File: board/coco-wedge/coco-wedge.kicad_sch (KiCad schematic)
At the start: 19 parts, among them J1 Foxconn_WQ21823-DES1-7F, J2 ZX-TYPEC-WCM1648, J3 Conn_ARM_JTAG_SWD_10, SW1 SW_Push, SW2 SW_SPDT, U1 AMS1117-3.3, U2 STM32G0B0RETx, U3 74LVC1G07, Y1 Crystal

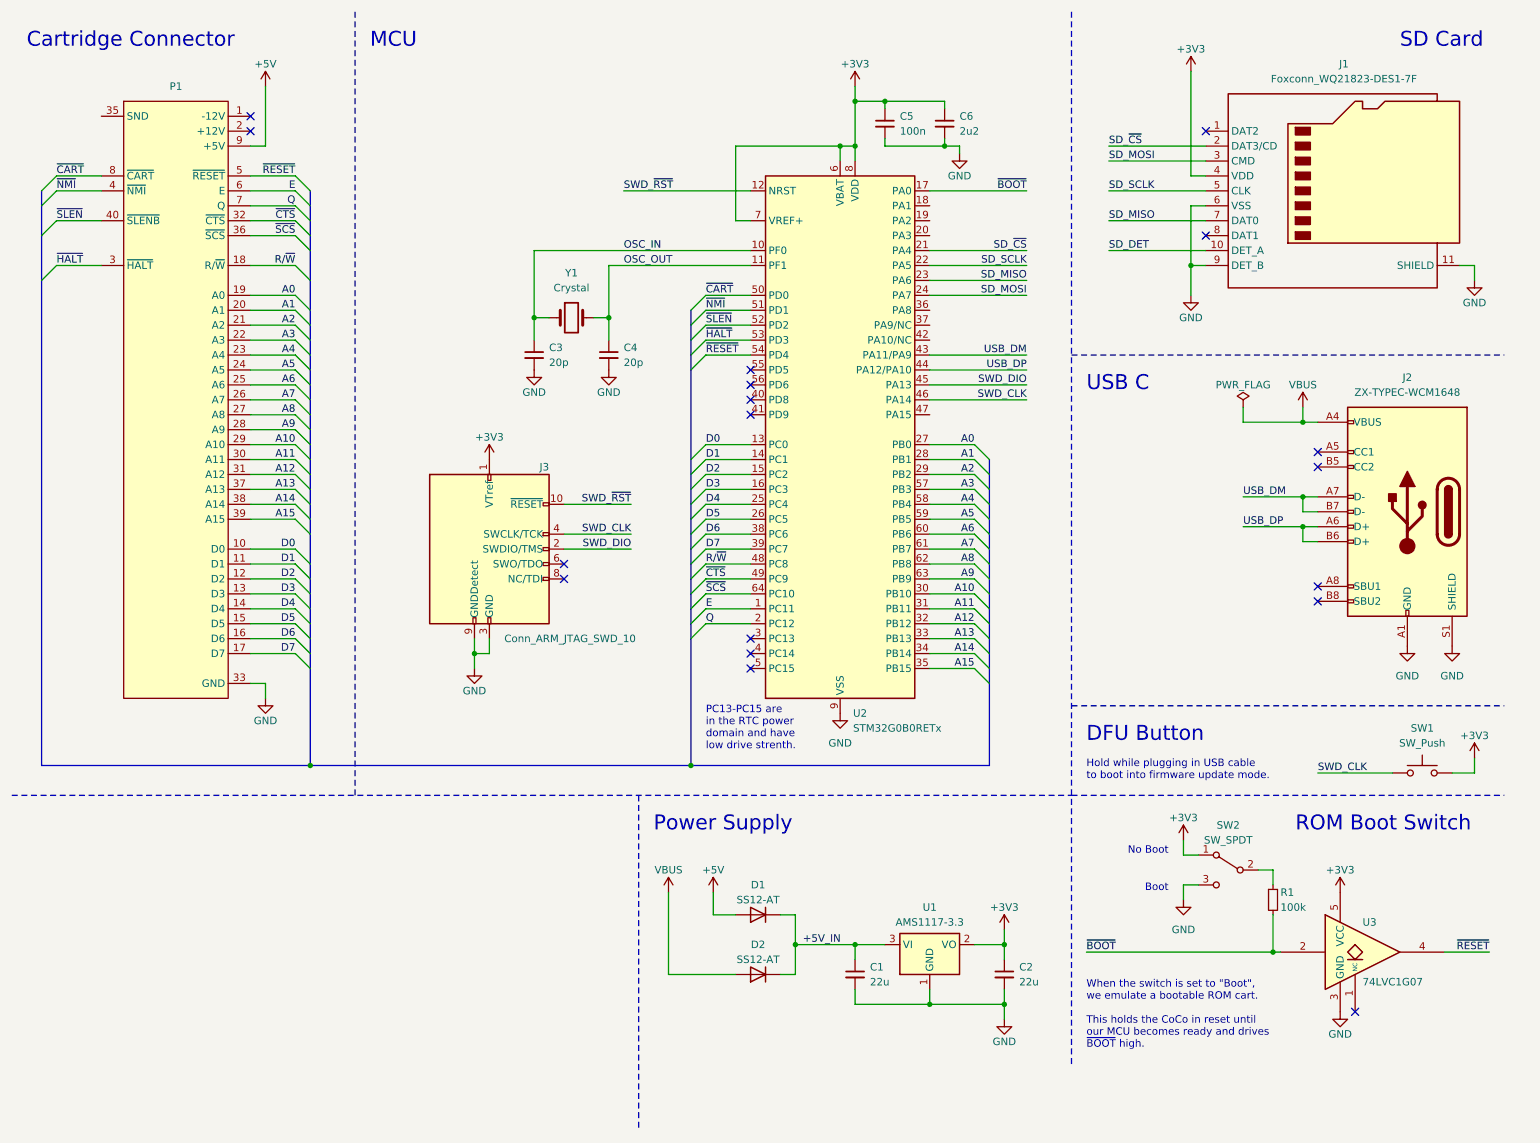
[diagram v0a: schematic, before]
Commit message: Add most of the audio system, do some routing.
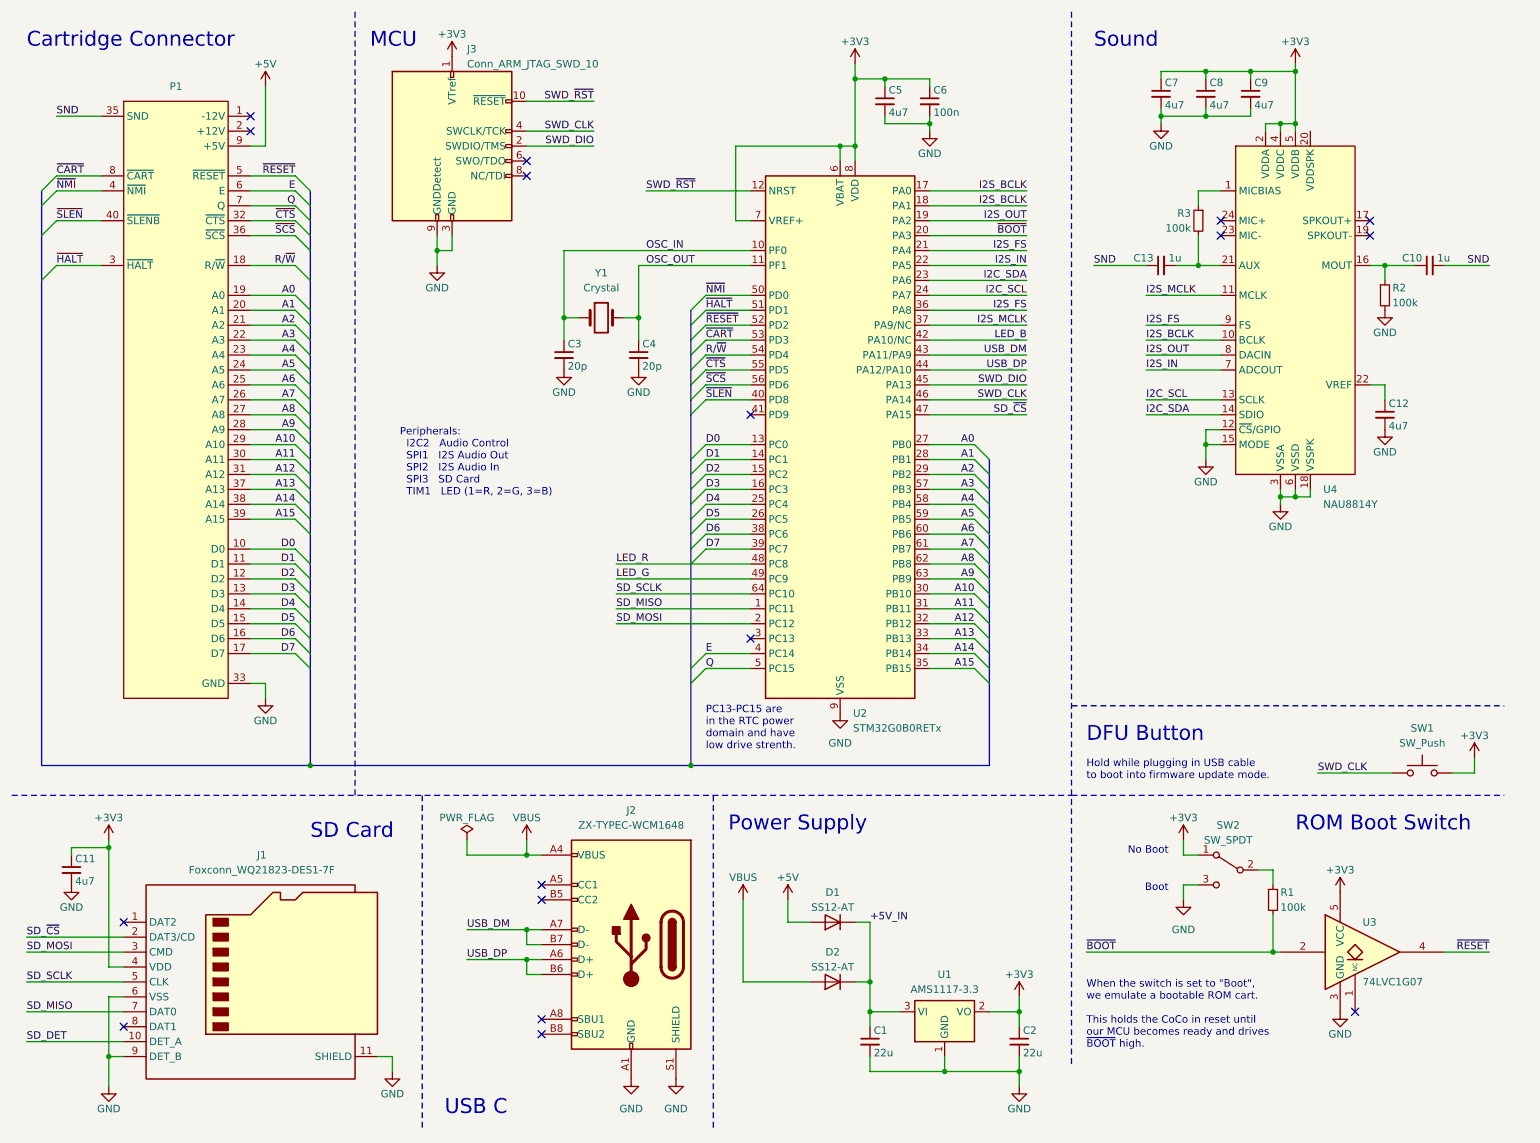
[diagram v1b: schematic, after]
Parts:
- added C10, C13: 1u, Capacitor_SMD:C_0603_1608Metric, symbol Device:C_Small
- added C11, C12, C7, C8, C9: 4u7, Capacitor_SMD:C_0603_1608Metric, symbol Device:C_Small
- added R2, R3: 100k, Resistor_SMD:R_0603_1608Metric, symbol Device:R_Small
- added U4: NAU8814Y, Package_DFN_QFN:VQFN-24-1EP_4x4mm_P0.5mm_EP2.5x2.5mm_ThermalVias, symbol 0Project:Nuvoton_NAU8814Y
- C5: value 100n -> 4u7
- C6: value 2u2 -> 100n
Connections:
- net +3V3: now also C11.1, C7.1, C8.1, C9.1, U4.2 (VDDA), U4.4 (VDDC), U4.5 (VDDB)
- net E: now also U2.4 (PC14); no longer U2.1 (PC11)
- net GND: now also C11.2, C12.2, C7.2, C8.2, C9.2, R2.2, U4.12 (~{CS}/GPIO), U4.15 (MODE), U4.18 (VSSPK), U4.25 (VSSA), U4.3 (VSSA), U4.6 (VSSD)
- net Q: now also U2.5 (PC15); no longer U2.2 (PC12)
- net R/~{W}: now also U2.54 (PD4); no longer U2.48 (PC8)
- net SD_MISO: now also U2.1 (PC11); no longer U2.23 (PA6)
- net SD_MOSI: now also U2.2 (PC12); no longer U2.24 (PA7)
- net SD_SCLK: now also U2.64 (PC10); no longer U2.22 (PA5)
- net SD_~{CS}: now also U2.47 (PA15); no longer U2.21 (PA4)
- net ~{BOOT}: now also U2.20 (PA3); no longer U2.17 (PA0)
- net ~{CART}: now also U2.53 (PD3); no longer U2.50 (PD0)
- net ~{CTS}: now also U2.55 (PD5); no longer U2.49 (PC9)
- net ~{HALT}: now also U2.51 (PD1); no longer U2.53 (PD3)
- net ~{NMI}: now also U2.50 (PD0); no longer U2.51 (PD1)
- net ~{RESET}: now also U2.52 (PD2); no longer U2.54 (PD4)
- net ~{SCS}: now also U2.56 (PD6); no longer U2.64 (PC10)
- net ~{SLEN}: now also U2.40 (PD8); no longer U2.52 (PD2)
- net I2S_BCLK: now reaches U2.18 (PA1)
- net I2S_BCLK: now also U2.17 (PA0), U4.10 (BCLK)
- net I2S_OUT: now reaches U2.19 (PA2)
- net I2S_OUT: now also U4.8 (DACIN)
- net I2S_FS: now reaches U2.36 (PA8)
- net I2S_FS: now also U2.21 (PA4), U4.9 (FS)
- net I2S_MCLK: now reaches U2.37 (PA9/NC)
- net I2S_MCLK: now also U4.11 (MCLK)
- net LED_B: now reaches U2.42 (PA10/NC)
- net SND: now reaches P1.35 (SND)
- net SND: now also C10.2, C13.1
- new net: C12.1, U4.22 (VREF)
- new net: C13.2, R3.2, U4.21 (AUX)
- new net: C10.1, R2.1, U4.16 (MOUT)
- new net: R3.1, U4.1 (MICBIAS)
- new net I2C_SCL: U2.24 (PA7), U4.13 (SCLK)
- new net I2C_SDA: U2.23 (PA6), U4.14 (SDIO)
- new net I2S_IN: U2.22 (PA5), U4.7 (ADCOUT)
- new net LED_G: U2.49 (PC9)
- new net LED_R: U2.48 (PC8)
- no-connect marks 18 -> 17
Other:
- note added: "Peripherals: I2C2 Audio Control SPI1 I2S Audio Out SPI2 I2S Audio In SPI3 SD Card TIM1 LED (1=R, 2=G, 3=B)"
- note added: "Sound"
- moved on the sheet: C1, C2, D1, D2, J1, J2, J3, U1, Y1
